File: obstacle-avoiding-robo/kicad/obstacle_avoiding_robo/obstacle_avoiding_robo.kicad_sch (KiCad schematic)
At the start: 6 parts, among them M1 Left Motor, M2 Right Motor, U1 TB6612FNG, U2 3.3V Ultrasonic Sensor

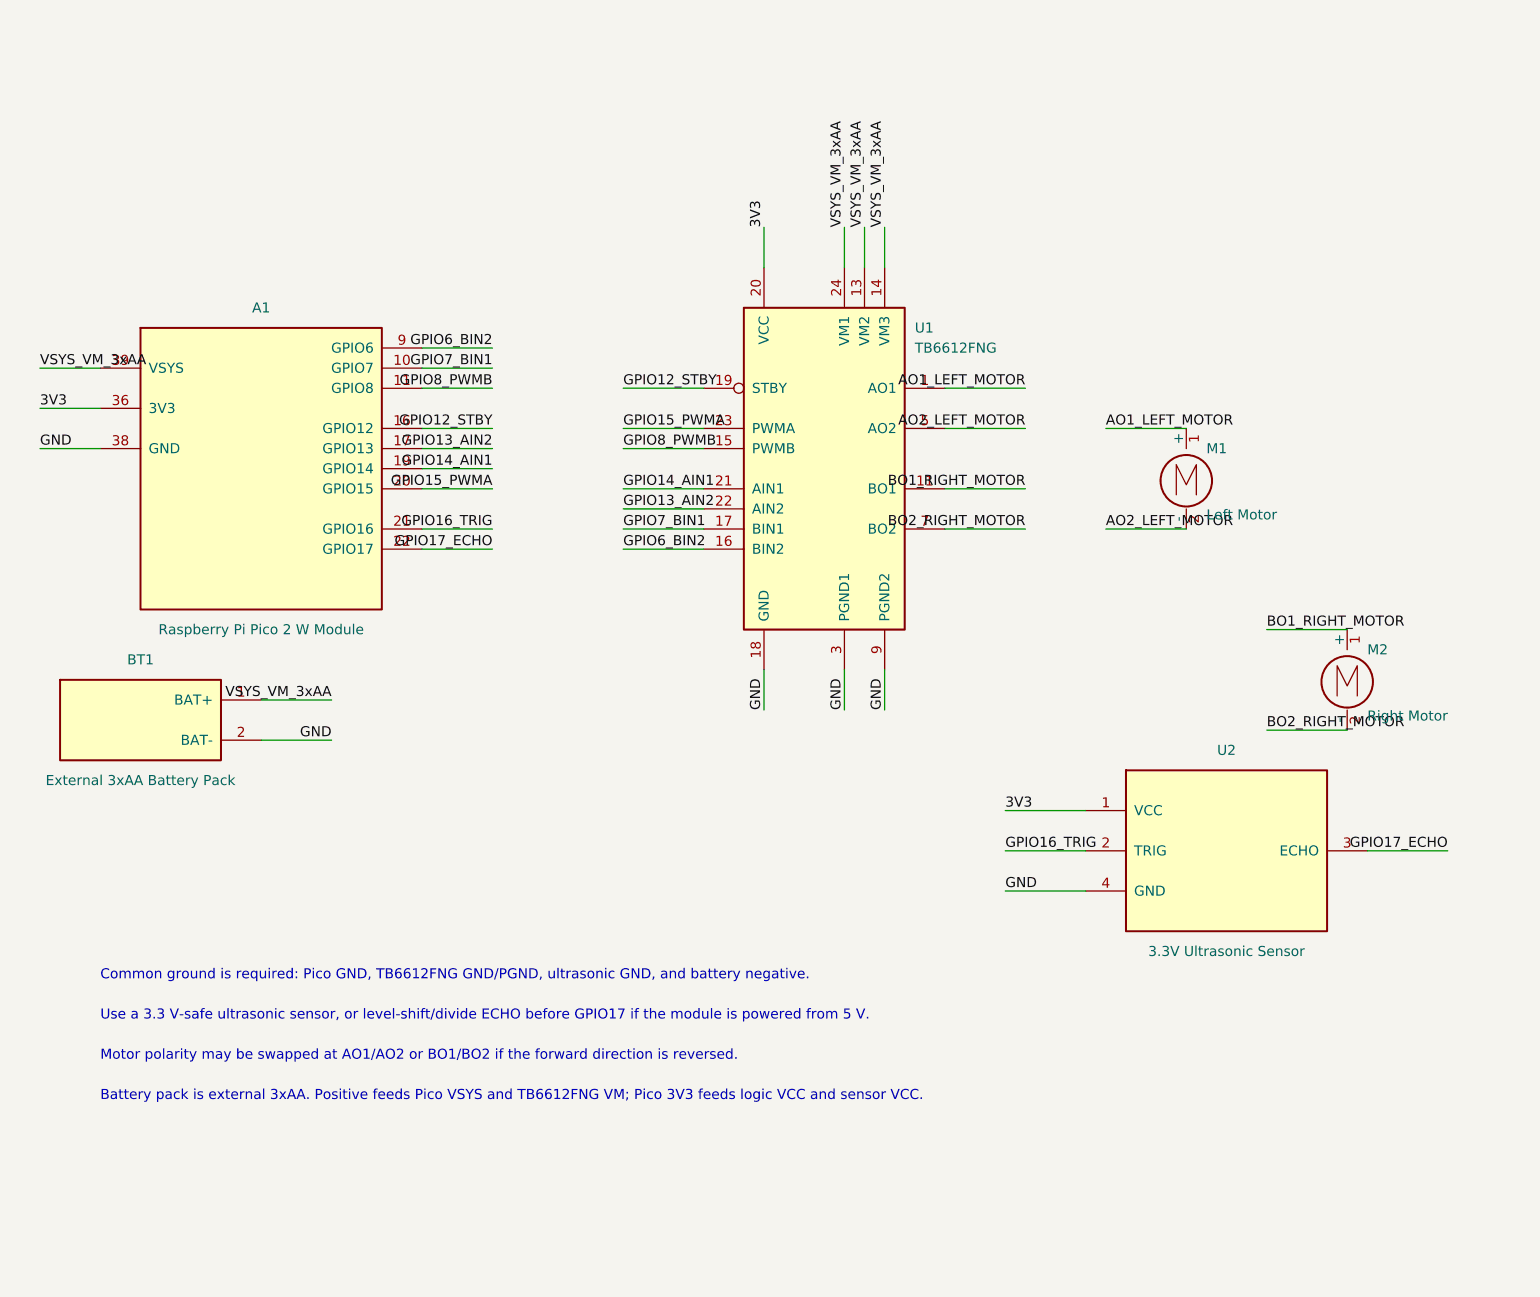
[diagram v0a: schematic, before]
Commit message: Step 2: PCB Ready schematic
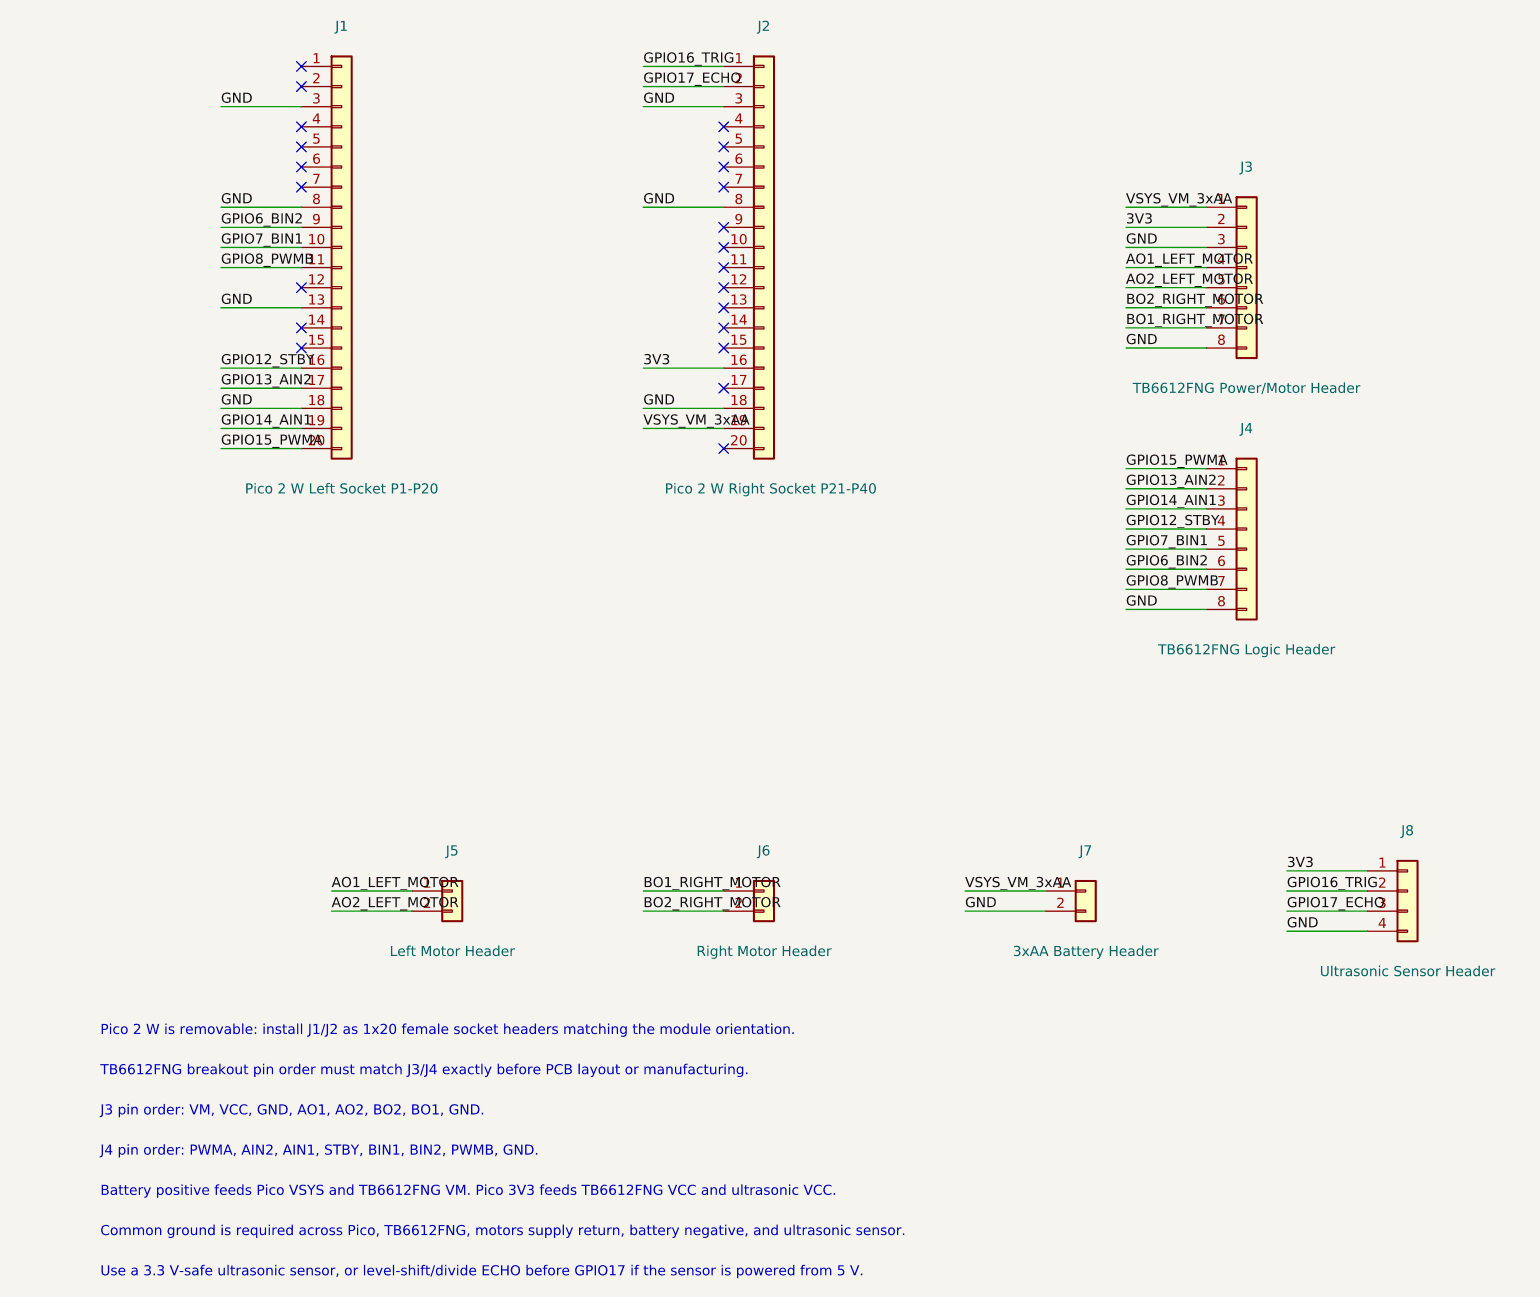
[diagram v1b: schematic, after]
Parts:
- removed A1: Raspberry Pi Pico 2 W Module, symbol obstacle_avoiding_robo:Raspberry_Pi_Pico_2_W_Module
- removed BT1: External 3xAA Battery Pack, symbol obstacle_avoiding_robo:Battery_3xAA
- removed M1: Left Motor, symbol Motor:Motor_DC
- removed M2: Right Motor, symbol Motor:Motor_DC
- removed U1: TB6612FNG, Package_SO:SSOP-24_5.3x8.2mm_P0.65mm, symbol Driver_Motor:TB6612FNG
- removed U2: 3.3V Ultrasonic Sensor, symbol obstacle_avoiding_robo:Ultrasonic_3V3
- added J1: Pico 2 W Left Socket P1-P20, Connector_PinSocket_2.54mm:PinSocket_1x20_P2.54mm_Vertical, symbol Connector_Generic:Conn_01x20
- added J2: Pico 2 W Right Socket P21-P40, Connector_PinSocket_2.54mm:PinSocket_1x20_P2.54mm_Vertical, symbol Connector_Generic:Conn_01x20
- added J3: TB6612FNG Power/Motor Header, Connector_PinHeader_2.54mm:PinHeader_1x08_P2.54mm_Vertical, symbol Connector_Generic:Conn_01x08
- added J4: TB6612FNG Logic Header, Connector_PinHeader_2.54mm:PinHeader_1x08_P2.54mm_Vertical, symbol Connector_Generic:Conn_01x08
- added J5: Left Motor Header, Connector_PinHeader_2.54mm:PinHeader_1x02_P2.54mm_Vertical, symbol Connector_Generic:Conn_01x02
- added J6: Right Motor Header, Connector_PinHeader_2.54mm:PinHeader_1x02_P2.54mm_Vertical, symbol Connector_Generic:Conn_01x02
- added J7: 3xAA Battery Header, Connector_PinHeader_2.54mm:PinHeader_1x02_P2.54mm_Vertical, symbol Connector_Generic:Conn_01x02
- added J8: Ultrasonic Sensor Header, Connector_PinHeader_2.54mm:PinHeader_1x04_P2.54mm_Vertical, symbol Connector_Generic:Conn_01x04
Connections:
- net 3V3: now also J2.16 (Pin_16), J3.2 (Pin_2), J8.1 (Pin_1)
- net AO1_LEFT_MOTOR: now also J3.4 (Pin_4), J5.1 (Pin_1)
- net AO2_LEFT_MOTOR: now also J3.5 (Pin_5), J5.2 (Pin_2)
- net BO1_RIGHT_MOTOR: now also J3.7 (Pin_7), J6.1 (Pin_1)
- net BO2_RIGHT_MOTOR: now also J3.6 (Pin_6), J6.2 (Pin_2)
- net GND: now also J1.13 (Pin_13), J1.18 (Pin_18), J1.3 (Pin_3), J1.8 (Pin_8), J2.18 (Pin_18), J2.3 (Pin_3), J2.8 (Pin_8), J3.3 (Pin_3), J3.8 (Pin_8), J4.8 (Pin_8), J7.2 (Pin_2), J8.4 (Pin_4)
- net GPIO12_STBY: now also J1.16 (Pin_16), J4.4 (Pin_4)
- net GPIO13_AIN2: now also J1.17 (Pin_17), J4.2 (Pin_2)
- net GPIO14_AIN1: now also J1.19 (Pin_19), J4.3 (Pin_3)
- net GPIO15_PWMA: now also J1.20 (Pin_20), J4.1 (Pin_1)
- net GPIO16_TRIG: now also J2.1 (Pin_1), J8.2 (Pin_2)
- net GPIO17_ECHO: now also J2.2 (Pin_2), J8.3 (Pin_3)
- net GPIO6_BIN2: now also J1.9 (Pin_9), J4.6 (Pin_6)
- net GPIO7_BIN1: now also J1.10 (Pin_10), J4.5 (Pin_5)
- net GPIO8_PWMB: now also J1.11 (Pin_11), J4.7 (Pin_7)
- net VSYS_VM_3xAA: now also J2.19 (Pin_19), J3.1 (Pin_1), J7.1 (Pin_1)
- no-connect marks 0 -> 22
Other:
- note added: "Battery positive feeds Pico VSYS and TB6612FNG VM. Pico 3V3 feeds TB6612FNG VCC and ultrasonic VCC."
- note added: "Common ground is required across Pico, TB6612FNG, motors supply return, battery negative, and ultrasonic sensor."
- note added: "J3 pin order: VM, VCC, GND, AO1, AO2, BO2, BO1, GND."
- note added: "J4 pin order: PWMA, AIN2, AIN1, STBY, BIN1, BIN2, PWMB, GND."
- note added: "Pico 2 W is removable: install J1/J2 as 1x20 female socket headers matching the module orientation."
- note added: "TB6612FNG breakout pin order must match J3/J4 exactly before PCB layout or manufacturing."
- note added: "Use a 3.3 V-safe ultrasonic sensor, or level-shift/divide ECHO before GPIO17 if the sensor is powered from 5 V."
- note removed: "Battery pack is external 3xAA. Positive feeds Pico VSYS and TB6612FNG VM; Pico 3V3 feeds logic VCC and sensor VCC."
- note removed: "Common ground is required: Pico GND, TB6612FNG GND/PGND, ultrasonic GND, and battery negative."
- note removed: "Motor polarity may be swapped at AO1/AO2 or BO1/BO2 if the forward direction is reversed."
- note removed: "Use a 3.3 V-safe ultrasonic sensor, or level-shift/divide ECHO before GPIO17 if the module is powered from 5 V."
- company: Raspberry Pi Pico 2 W + TB6612FNG -> Raspberry Pi Pico 2 W + TB6612FNG Breakout
- title: Obstacle-Avoiding Robo Car - Dual Motor Wiring -> Obstacle-Avoiding Robo Car - Carrier Board Schematic
